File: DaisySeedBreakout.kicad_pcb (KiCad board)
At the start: 2 copper layers, 56.1 x 65 mm, 185 parts, among them J10 Conn_01x03, J11 Conn_01x03, J12 Conn_01x03, J13 Conn_01x03, J14 Conn_01x03, J15 Conn_02x08, J16 Conn_01x03, J17 Conn_01x03, J19 Conn_01x03, J2 Conn_02x08, J20 Conn_01x03, J21 Conn_01x03, J22 Conn_01x03, J23 Conn_01x03, J24 Conn_01x02, J25 Conn_01x02, J26 Conn_02x04, J28 Conn_01x03, J29 Conn_01x03, J3 Conn_01x03, J30 Conn_01x02, J31 Conn_02x04, J32 Conn_01x02, J33 Conn_01x02, J34 Conn_01x02, J35 Conn_01x02, J36 MJ-3523-SMT-TR, J37 MJ-3523-SMT-TR, J38 MJ-3523-SMT-TR, J39 MJ-3523-SMT-TR, J4 5027740891, J40 MJ-3523-SMT-TR, J41 MJ-3523-SMT-TR, J42 MJ-3523-SMT-TR, J43 MJ-3523-SMT-TR, J44 MJ-3523-SMT-TR, J45 MJ-3523-SMT-TR, J46 Conn_01x02, J5 Conn_02x08, J6 Conn_01x02, J7 Conn_01x03, J8 Conn_01x03, J9 Conn_01x03, U1 TCA6424ARGJR, U2 H11L1M, U5 MAX9814

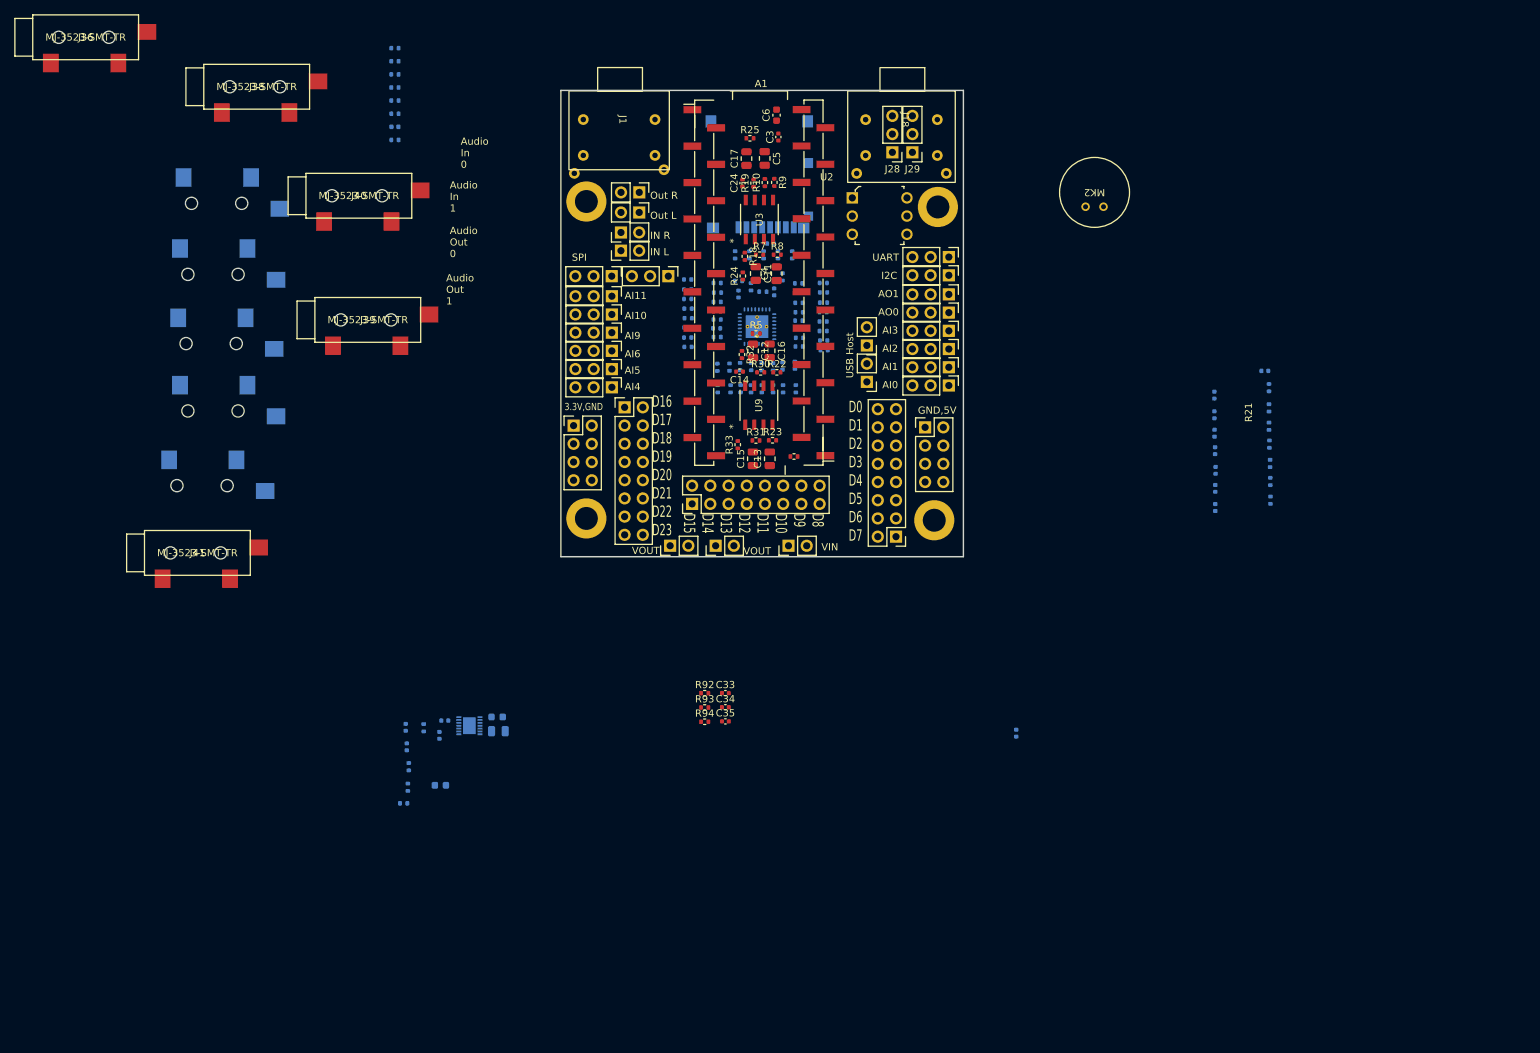
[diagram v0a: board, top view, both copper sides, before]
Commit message: Converted circuits to sub circuits.  Removed MIDI connector, changed to header only
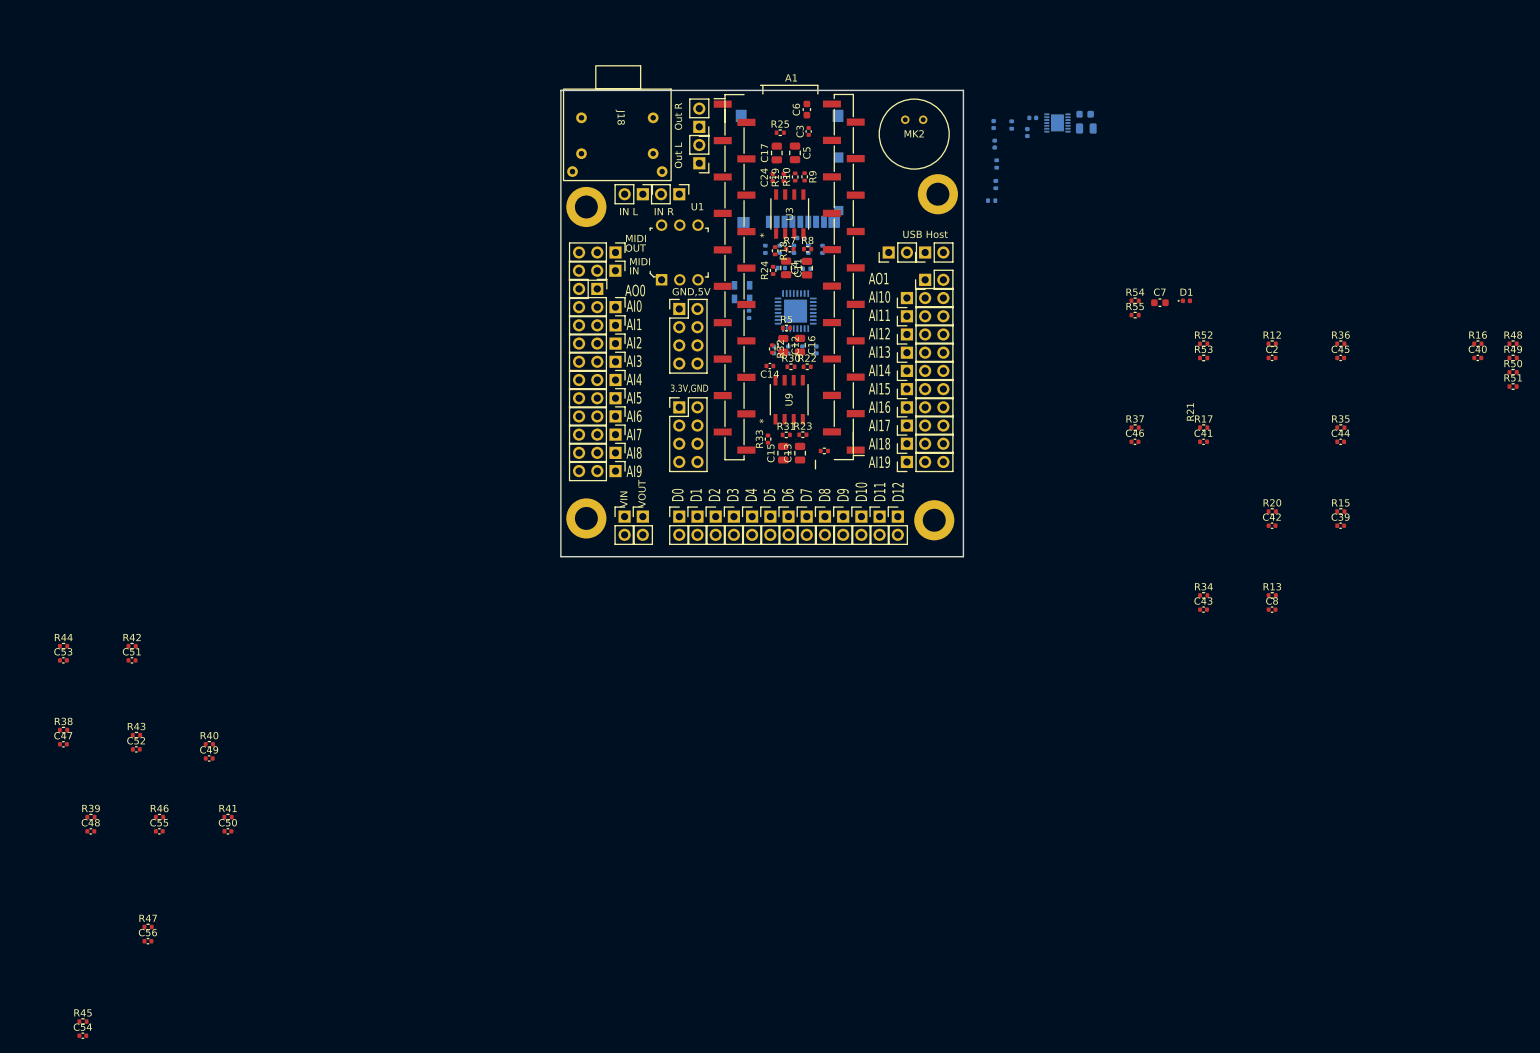
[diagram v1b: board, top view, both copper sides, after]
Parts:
- removed C10, C25, C27, C28, C33, C34, C35, C9: SPARE, Capacitor_SMD:C_0402_1005Metric
- removed C26, C29, C30: 0.1uF, Capacitor_SMD:C_0402_1005Metric
- removed C32: 0.1uF, Capacitor_SMD:C_0603_1608Metric
- removed J15, J2, J5: Conn_02x08, Ultralibrarian:PinHeader_2x08_P2.54mm_Vertical_Female
- removed J16, J17, J19, J23, J28, J29, J7: Conn_01x03, Ultralibrarian:PinHeader_1x03_P2.54mm_Vertical_Female
- removed J36, J37, J38, J39, J40, J41, J42, J43, J44, J45: MJ-3523-SMT-TR, SurfaceMountAudiofootprints:MJ-3523-SMT-TR
- removed J46: Conn_01x02, Connector_PinHeader_2.54mm:PinHeader_1x02_P2.54mm_Vertical
- removed R56, R57, R58, R59, R60, R61, R62, R63, R64, R65, R66, R67, R68, R69: 499, Resistor_SMD:R_0402_1005Metric
- removed R70, R71, R72, R73, R74, R75, R76, R77: 22k, Resistor_SMD:R_0402_1005Metric
- removed R78, R79, R80, R81, R82, R83, R84, R92, R93, R94: 1k, Resistor_SMD:R_0402_1005Metric
- removed R85: 220, Resistor_SMD:R_0402_1005Metric
- removed R86, R87: SPARE, Resistor_SMD:R_0402_1005Metric
- removed R88: 0, Resistor_SMD:R_0402_1005Metric
- removed R89: 270, Resistor_SMD:R_0402_1005Metric
- removed R90: 10, Resistor_SMD:R_0402_1005Metric
- removed R91: 33, Resistor_SMD:R_0402_1005Metric
- removed U2: H11L1M, digikey-footprints:DIP-6_W7.62mm
- added C31: 0.1uF, Capacitor_SMD:C_0402_1005Metric, B.Cu at (137.7, 68.2)
- added C36: 0.1uF, Capacitor_SMD:C_0402_1005Metric, B.Cu at (139.7, 68.2)
- added C37: 0.1uF, Capacitor_SMD:C_0402_1005Metric, B.Cu at (141.6, 68.2)
- added C38: 0.1uF, Capacitor_SMD:C_0402_1005Metric, B.Cu at (143.6, 68.2)
- added C39: SPARE, Capacitor_SMD:C_0402_1005Metric, F.Cu at (216.7, 92.7)
- added C40: SPARE, Capacitor_SMD:C_0402_1005Metric, F.Cu at (235.8, 69.3)
- added C41: SPARE, Capacitor_SMD:C_0402_1005Metric, F.Cu at (197.6, 81.0)
- added C42: SPARE, Capacitor_SMD:C_0402_1005Metric, F.Cu at (207.1, 92.7)
- added C43: SPARE, Capacitor_SMD:C_0402_1005Metric, F.Cu at (197.6, 104.4)
- added C44: SPARE, Capacitor_SMD:C_0402_1005Metric, F.Cu at (216.7, 81.0)
- added C45: SPARE, Capacitor_SMD:C_0402_1005Metric, F.Cu at (216.7, 69.3)
- added C46: SPARE, Capacitor_SMD:C_0402_1005Metric, F.Cu at (188.0, 81.0)
- added C47: SPARE, Capacitor_SMD:C_0402_1005Metric, F.Cu at (38.6, 123.2)
- added C48: SPARE, Capacitor_SMD:C_0402_1005Metric, F.Cu at (42.4, 135.3)
- added C49: SPARE, Capacitor_SMD:C_0402_1005Metric, F.Cu at (58.9, 125.2)
- added C50: SPARE, Capacitor_SMD:C_0402_1005Metric, F.Cu at (61.5, 135.3)
- added C51: SPARE, Capacitor_SMD:C_0402_1005Metric, F.Cu at (48.1, 111.5)
- added C52: SPARE, Capacitor_SMD:C_0402_1005Metric, F.Cu at (48.8, 123.9)
- added C53: SPARE, Capacitor_SMD:C_0402_1005Metric, F.Cu at (38.6, 111.5)
- added C54: SPARE, Capacitor_SMD:C_0402_1005Metric, F.Cu at (41.3, 163.8)
- added C55: SPARE, Capacitor_SMD:C_0402_1005Metric, F.Cu at (52.0, 135.3)
- added C56: SPARE, Capacitor_SMD:C_0402_1005Metric, F.Cu at (50.4, 150.7)
- added J27: Conn_01x03, Ultralibrarian:PinHeader_1x03_P2.54mm_Vertical_Female, F.Cu at (115.6, 85.1)
- added J47: Conn_01x03, Ultralibrarian:PinHeader_1x03_P2.54mm_Vertical_Female, F.Cu at (115.6, 80.0)
- added J48: Conn_01x03, Ultralibrarian:PinHeader_1x03_P2.54mm_Vertical_Female, F.Cu at (115.6, 77.5)
- added J49: Conn_01x03, Ultralibrarian:PinHeader_1x03_P2.54mm_Vertical_Female, F.Cu at (156.2, 68.6)
- added J50: Conn_01x03, Ultralibrarian:PinHeader_1x03_P2.54mm_Vertical_Female, F.Cu at (156.2, 63.5)
- added J51: Conn_01x03, Ultralibrarian:PinHeader_1x03_P2.54mm_Vertical_Female, F.Cu at (115.6, 74.9)
- added J52: Conn_01x03, Ultralibrarian:PinHeader_1x03_P2.54mm_Vertical_Female, F.Cu at (115.6, 82.5)
- added J53: Conn_01x03, Ultralibrarian:PinHeader_1x03_P2.54mm_Vertical_Female, F.Cu at (156.2, 61.0)
- added J54: Conn_01x03, Ultralibrarian:PinHeader_1x03_P2.54mm_Vertical_Female, F.Cu at (156.2, 71.1)
- added J55: Conn_01x03, Ultralibrarian:PinHeader_1x03_P2.54mm_Vertical_Female, F.Cu at (156.2, 66.0)
- added J56: Conn_01x03, Ultralibrarian:PinHeader_1x03_P2.54mm_Vertical_Female, F.Cu at (115.6, 69.8)
- added J57: Conn_01x03, Ultralibrarian:PinHeader_1x03_P2.54mm_Vertical_Female, F.Cu at (156.2, 78.7)
- added J58: Conn_01x03, Ultralibrarian:PinHeader_1x03_P2.54mm_Vertical_Female, F.Cu at (156.2, 73.7)
- added J59: Conn_01x03, Ultralibrarian:PinHeader_1x03_P2.54mm_Vertical_Female, F.Cu at (156.2, 76.2)
- added J60: Conn_01x03, Ultralibrarian:PinHeader_1x03_P2.54mm_Vertical_Female, F.Cu at (115.6, 64.8)
- added J61: Conn_01x03, Ultralibrarian:PinHeader_1x03_P2.54mm_Vertical_Female, F.Cu at (115.6, 62.2)
- added J62: Conn_01x03, Ultralibrarian:PinHeader_1x03_P2.54mm_Vertical_Female, F.Cu at (115.6, 67.3)
- added J63: Conn_01x03, Ultralibrarian:PinHeader_1x03_P2.54mm_Vertical_Female, F.Cu at (115.6, 72.4)
- added J64: Conn_01x03, Ultralibrarian:PinHeader_1x03_P2.54mm_Vertical_Female, F.Cu at (156.2, 83.8)
- added J65: Conn_01x03, Ultralibrarian:PinHeader_1x03_P2.54mm_Vertical_Female, F.Cu at (156.2, 81.3)
- added J66: Conn_01x02, Ultralibrarian:PinHeader_1x02_P2.54mm_Vertical_Female, F.Cu at (152.4, 91.4)
- added J67: Conn_01x02, Ultralibrarian:PinHeader_1x02_P2.54mm_Vertical_Female, F.Cu at (147.3, 91.4)
- added J68: Conn_01x02, Ultralibrarian:PinHeader_1x02_P2.54mm_Vertical_Female, F.Cu at (142.2, 91.4)
- added J69: Conn_01x02, Ultralibrarian:PinHeader_1x02_P2.54mm_Vertical_Female, F.Cu at (158.8, 58.4)
- added J70: Conn_01x02, Ultralibrarian:PinHeader_1x02_P2.54mm_Vertical_Female, F.Cu at (113.0, 59.7)
- added R95: 33.2, Resistor_SMD:R_0402_1005Metric, B.Cu at (134.2, 63.2)
- added U4: ATMEGA1608-MFR, atmega:VQFN32_RXB_MCH-M, B.Cu at (140.7, 62.8)
- added U6: DSC6001CE2A-010.0000, oscillator:DFN4_3.2X2.5_MCH, B.Cu at (133.2, 60.1)
- C2, C8: value 0.1uF -> SPARE; moved to F.Cu
- C7: value SPARE -> 0.1uF; footprint Capacitor_SMD:C_0402_1005Metric -> Capacitor_SMD:C_0603_1608Metric; moved to F.Cu
- D1: moved to F.Cu
- J1: value ~ -> Conn_01x03; footprint Ultralibrarian:STX-4235-3-3-N -> Ultralibrarian:PinHeader_1x03_P2.54mm_Vertical_Female
- J10, J11, J12, J13, J14, J20, J21, J22, J8, J9: value Conn_01x03 -> Conn_01x02; footprint Ultralibrarian:PinHeader_1x03_P2.54mm_Vertical_Female -> Ultralibrarian:PinHeader_1x02_P2.54mm_Vertical_Female
- J32, J33, J34, J35: footprint Connector_PinHeader_2.54mm:PinHeader_1x02_P2.54mm_Vertical -> Ultralibrarian:PinHeader_1x02_P2.54mm_Vertical_Female
- R12, R13: value 47k -> 1k; moved to F.Cu
- R15, R16, R17, R20, R34, R35, R36, R37, R38, R39, R40, R41, R42, R43, R44, R45: value 22k -> 1k; moved to F.Cu
- R46, R47: value 499 -> 1k; moved to F.Cu
- R48, R49, R50, R51: value 499 -> 10k; moved to F.Cu
- R52: value 499 -> 10; moved to F.Cu
- R53: value 499 -> 33; moved to F.Cu
- R54: value 499 -> 220; moved to F.Cu
- R55: value 499 -> 270; moved to F.Cu
- U1: value TCA6424ARGJR -> H11L1M; footprint I2C Expander:RGJ0032A -> digikey-footprints:DIP-6_W7.62mm; moved to F.Cu
- moved R47 126.7 mm to (50.4, 148.7)
- moved R45 125.0 mm to (41.3, 161.8), turned to 0 degrees
- moved C23 117.4 mm to (181.2, 37.3)
- moved C18 117.4 mm to (173.0, 37.9)
- moved C19 117.4 mm to (168.3, 36.8)
- moved C20 117.4 mm to (181.1, 35.3)
- moved C21 117.4 mm to (168.5, 39.5)
- moved C22 117.4 mm to (173.8, 35.8)
- moved R26 117.4 mm to (168.6, 45.1)
- moved R27 117.4 mm to (168.0, 47.4)
- moved R28 117.4 mm to (168.7, 42.3)
- moved R29 117.4 mm to (170.8, 36.8)
- moved U5 117.4 mm to (177.2, 36.5)
- moved R46 116.1 mm to (52.0, 133.3)
- moved R39 113.5 mm to (42.4, 133.3), turned to 0 degrees
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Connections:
- A1 pad 10: unconnected-(A1-SPI1_POCI-Pad10) -> /arduino_coprocessor/UART0_RXD_SPI0_MISO
- A1 pad 11: unconnected-(A1-SPI1_PICO-Pad11) -> /arduino_coprocessor/UART0_TXD_SPI0_MOSI
- A1 pad 12: /I2C 24 GPIO/SCL -> /GPIO_Conn11/GPIO_Conn
- A1 pad 13: /I2C 24 GPIO/SDA -> /GPIO_Conn12/GPIO_Conn
- A1 pad 29: unconnected-(A1-DAC_OUT2-Pad29) -> /Analog_out_conn/AO_Conn
- A1 pad 30: unconnected-(A1-DAC_OUT1-Pad30) -> /Analog_out_conn1/AO_Conn
- A1 pad 33: unconnected-(A1-SAI2_SD_A-Pad33) -> /RESET_n
- A1 pad 34: unconnected-(A1-SAI2_FS-Pad34) -> /UPDI
- A1 pad 8: unconnected-(A1-SPI1_CS-Pad8) -> /arduino_coprocessor/SPI0_CS
- A1 pad 9: unconnected-(A1-SPI1_SCK-Pad9) -> /arduino_coprocessor/SPI0_SCLK
- C2 pad 1: +3.3V -> /AI0
- C7 pad 1: /AI0 -> +3.3V
- C8 pad 1: +3.3V -> /AI1
- J10 pad 1: GND -> /GPIO_Conn3/GPIO_Conn
- J10 pad 2: +3.3V -> GND
- J11 pad 1: GND -> /GPIO_Conn/GPIO_Conn
- J11 pad 2: +3.3V -> GND
- J12 pad 1: GND -> /GPIO_Conn7/GPIO_Conn
- J12 pad 2: +3.3V -> GND
- J13 pad 1: GND -> /GPIO_Conn4/GPIO_Conn
- J13 pad 2: +3.3V -> GND
- J14 pad 1: GND -> /GPIO_Conn5/GPIO_Conn
- J14 pad 2: +3.3V -> GND
- J20 pad 1: GND -> /GPIO_Conn6/GPIO_Conn
- J20 pad 2: +3.3V -> GND
- J21 pad 1: GND -> /GPIO_Conn8/GPIO_Conn
- J21 pad 2: +3.3V -> GND
- J22 pad 1: GND -> /GPIO_Conn9/GPIO_Conn
- J22 pad 2: +3.3V -> GND
- J3 pad 1: unconnected-(J3-Pin_1-Pad1) -> Net-(J3-Pin_1)
- J3 pad 2: unconnected-(J3-Pin_2-Pad2) -> Net-(D1-A)
- J3 pad 3: unconnected-(J3-Pin_3-Pad3) -> GND
- J8 pad 1: GND -> /GPIO_Conn1/GPIO_Conn
- J8 pad 2: +3.3V -> GND
- J9 pad 1: GND -> /GPIO_Conn2/GPIO_Conn
- J9 pad 2: +3.3V -> GND
- R11 pad 2: /I2C 24 GPIO/SCL -> /GPIO_Conn11/GPIO_Conn
- R12 pad 1: +3.3V -> /AI0
- R12 pad 2: /I2C 24 GPIO/INT_N -> Net-(J27-Pin_2)
- R13 pad 1: +3.3V -> /AI1
- R13 pad 2: /I2C 24 GPIO/RESET_N -> Net-(J47-Pin_2)
- R15 pad 1: +3.3V -> /AI2
- R15 pad 2: /I2C 24 GPIO/A0 -> Net-(J48-Pin_2)
- R16 pad 1: +3.3V -> /AI3
- R16 pad 2: /I2C 24 GPIO/A1 -> Net-(J49-Pin_2)
- R17 pad 1: +3.3V -> /AI4
- R17 pad 2: /I2C 24 GPIO/A2 -> Net-(J50-Pin_2)
- R20 pad 1: +3.3V -> /AI5
- R20 pad 2: /I2C 24 GPIO/A3 -> Net-(J51-Pin_2)
- R34 pad 1: +3.3V -> /AI6
- R34 pad 2: /I2C 24 GPIO/A4 -> Net-(J52-Pin_2)
- R35 pad 1: +3.3V -> /AI9
- R35 pad 2: /I2C 24 GPIO/A5 -> Net-(J53-Pin_2)
- R36 pad 1: +3.3V -> /AI10
- R36 pad 2: /I2C 24 GPIO/A6 -> Net-(J54-Pin_2)
- R37 pad 1: +3.3V -> /AI11
- R37 pad 2: /I2C 24 GPIO/A7 -> Net-(J55-Pin_2)
- R38 pad 1: +3.3V -> /AI_GPIO13/AI_GPIO
- R38 pad 2: /I2C 24 GPIO/B0 -> Net-(J56-Pin_2)
- R39 pad 1: +3.3V -> /AI_GPIO10/AI_GPIO
- R39 pad 2: /I2C 24 GPIO/B1 -> Net-(J57-Pin_2)
- R40 pad 1: +3.3V -> /AI_GPIO14/AI_GPIO
- R40 pad 2: /I2C 24 GPIO/B2 -> Net-(J58-Pin_2)
- R41 pad 1: +3.3V -> /AI_GPIO11/AI_GPIO
- R41 pad 2: /I2C 24 GPIO/B3 -> Net-(J59-Pin_2)
- R42 pad 1: +3.3V -> /AI_GPIO12/AI_GPIO
- R42 pad 2: /I2C 24 GPIO/B4 -> Net-(J60-Pin_2)
- R43 pad 1: +3.3V -> /AI_GPIO15/AI_GPIO
- R43 pad 2: /I2C 24 GPIO/B5 -> Net-(J61-Pin_2)
- R44 pad 1: +3.3V -> /AI_GPIO17/AI_GPIO
- R44 pad 2: /I2C 24 GPIO/B6 -> Net-(J62-Pin_2)
- R45 pad 1: +3.3V -> /AI_GPIO19/AI_GPIO
- R45 pad 2: /I2C 24 GPIO/B7 -> Net-(J63-Pin_2)
- R46 pad 1: Net-(U1-P00) -> /AI_GPIO18/AI_GPIO
- R46 pad 2: /I2C 24 GPIO/A0 -> Net-(J64-Pin_2)
- R47 pad 1: Net-(U1-P01) -> /AI_GPIO16/AI_GPIO
- R47 pad 2: /I2C 24 GPIO/A1 -> Net-(J65-Pin_2)
- R48 pad 1: Net-(U1-P02) -> +3.3V
- R48 pad 2: /I2C 24 GPIO/A2 -> /GPIO_Conn3/GPIO_Conn
- R49 pad 1: Net-(U1-P03) -> +3.3V
- R49 pad 2: /I2C 24 GPIO/A3 -> /GPIO_Conn2/GPIO_Conn
- R50 pad 1: Net-(U1-P04) -> +3.3V
- R50 pad 2: /I2C 24 GPIO/A4 -> /GPIO_Conn1/GPIO_Conn
- R51 pad 1: Net-(U1-P05) -> +3.3V
- R51 pad 2: /I2C 24 GPIO/A5 -> /GPIO_Conn/GPIO_Conn
- R52 pad 1: Net-(U1-P06) -> /MIDI_UART_TX
- R52 pad 2: /I2C 24 GPIO/A6 -> Net-(J1-Pin_2)
- R53 pad 1: Net-(U1-P07) -> +3.3V
- R53 pad 2: /I2C 24 GPIO/A7 -> Net-(J1-Pin_1)
- R54 pad 1: Net-(U1-P10) -> Net-(D1-K)
- R54 pad 2: /I2C 24 GPIO/B0 -> Net-(J3-Pin_1)
- R55 pad 1: Net-(U1-P11) -> /MIDI_UART_RX
- R55 pad 2: /I2C 24 GPIO/B1 -> +3.3V
- R6 pad 2: /I2C 24 GPIO/SDA -> /GPIO_Conn12/GPIO_Conn
- U1 pad 1: Net-(U1-P00) -> Net-(D1-K)
- U1 pad 2: Net-(U1-P01) -> Net-(D1-A)
- U1 pad 3: Net-(U1-P02) -> unconnected-(U1-NC-Pad3)
- U1 pad 4: Net-(U1-P03) -> /MIDI_UART_RX
- U1 pad 5: Net-(U1-P04) -> GND
- U1 pad 6: Net-(U1-P05) -> +3.3V
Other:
- board text added: "AI0 AI1 AI2 AI3 AI4 AI5 AI6 AI7 AI8 AI9"
- board text added: "AO1 AI10 AI11 AI12 AI13 AI14 AI15 AI16 AI17 AI18 AI19"
- board text added: "D0 D1 D2 D3 D4 D5 D6 D7 D8 D9 D10 D11 D12"
- board text added: "IN"
- board text added: "MIDI"
- board text added: "OUT"
- board text removed: "AI0"
- board text removed: "AI1"
- board text removed: "AI10"
- board text removed: "AI11"
- board text removed: "AI2"
- board text removed: "AI3"
- board text removed: "AI4"
- board text removed: "AI5"
- board text removed: "AI6"
- board text removed: "AI9"
- board text removed: "AO1"
- board text removed: "Audio In 0"
- board text removed: "Audio In 1"
- board text removed: "Audio Out 0"
- board text removed: "Audio Out 1"
- board text removed: "D0 D1 D2 D3 D4 D5 D6 D7"
- board text removed: "D16 D17 D18 D19 D20 D21 D22 D23"
- board text removed: "D8 D9 D10 D11 D12 D13 D14 D15"
- board text removed: "I2C"
- board text removed: "SPI"
- board text removed: "UART"

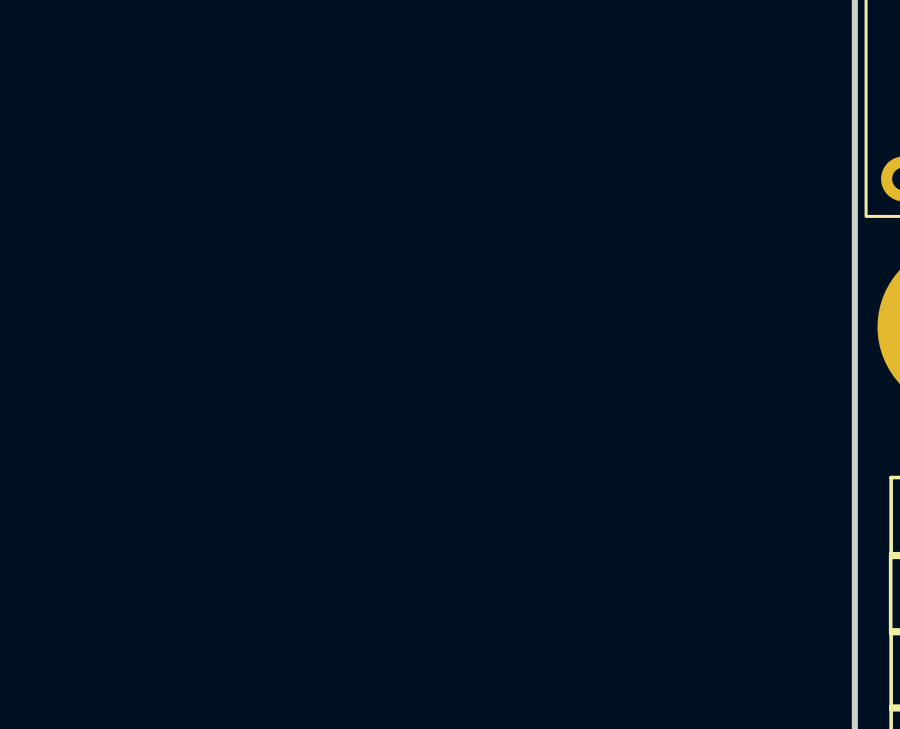
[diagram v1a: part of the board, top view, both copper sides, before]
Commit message: Placeholder for speaker driver
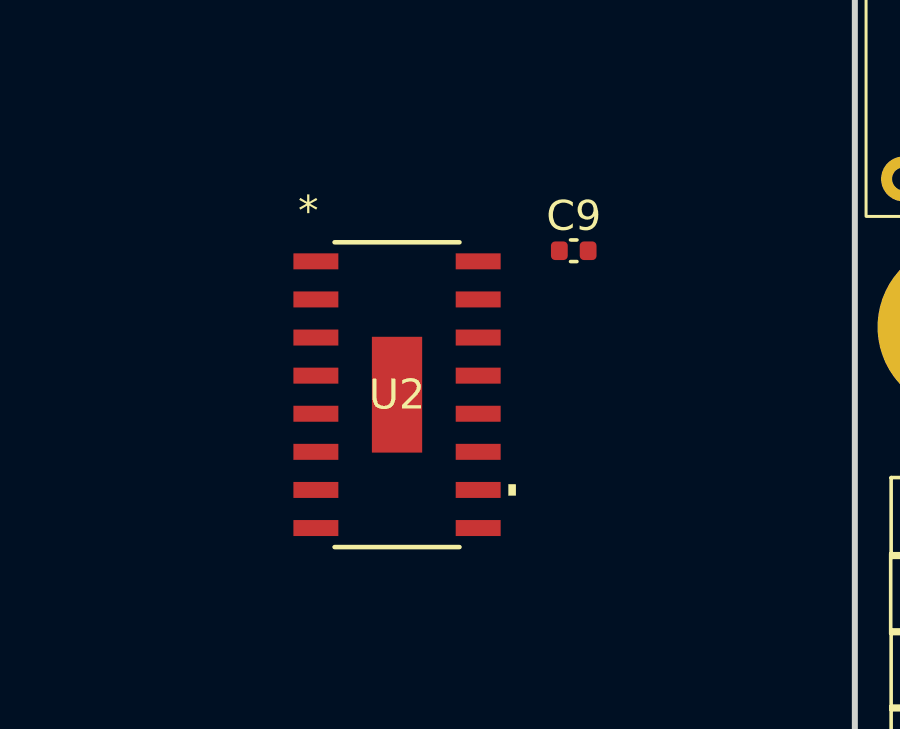
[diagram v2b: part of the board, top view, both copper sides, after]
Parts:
- added C9: 0.1uF, Capacitor_SMD:C_0402_1005Metric, F.Cu at (98.6, 45.7)
- added U2: PAM8320RDR, PAM8320:SO-16EP_3P9X9P9_DIO, F.Cu at (92.7, 50.5)
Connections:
- net /Analog_out_conn/AO_Conn renamed /AO0
- net /Analog_out_conn1/AO_Conn renamed /AO1
- A1 pad 21: unconnected-(A1-3V3_A-Pad21) -> Net-(A1-3V3_A)
